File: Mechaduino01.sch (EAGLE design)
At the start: 68 parts, among them IC1 SAMD21G18A-AUT, IC2 AP2112K-3.3, Q1 2.5A/30V, Q2 NFET, Q3 BSS138, Q4 BSS138, SW1 SPST_TACT-KMR2, U3 74AHC1G125, Y1 32,768Khz

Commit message: Final
ordered
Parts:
- removed SW1: SPST_TACT-KMR2, adafruit:SPST_TACT-KMR2
- added SW2: (no value), MF_Switches:TACT_4.2MM
- C10, C18: device swift:CAP0402 -> rcl:C-USC0805
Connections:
- net GND: now also SW2.P$3, SW2.P$4; no longer SW1.P, SW1.P1
- net RESET: now also SW2.P$1, SW2.P$2; no longer SW1.S, SW1.S1
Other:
- moved on the sheet: C10, C18
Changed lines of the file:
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@@
 <part name="C4" library="swift" deviceset="CAP" device="0402" value="0.1uF"/>
 <part name="GND6" library="PowerTags" deviceset="GND" device=""/>
-<part name="SW1" library="adafruit" deviceset="SPST_TACT" device="-KMR2" value=""/>
 <part name="GND11" library="supply1" deviceset="GND" device=""/>
 <part name="D1" library="adafruit" deviceset="DIODE" device="SOD-523"/>
@@
 <part name="IC2" library="SparkFun-PowerIC" deviceset="AP2202-ADJ" device="" value="AP2112K-3.3"/>
 <part name="C9" library="swift" deviceset="CAP" device="0402" value="0.1uF"/>
-<part name="C10" library="swift" deviceset="CAP" device="0402" value="10.0uF"/>
+<part name="C10" library="rcl" deviceset="C-US" device="C0805" value="10.0uF"/>
 <part name="GND5" library="supply1" deviceset="GND" device=""/>
 <part name="GND7" library="supply1" deviceset="GND" device=""/>
@@
 <part name="R21" library="adafruit" deviceset="R-US_" device="R0402-VISHAY" value="10K"/>
 <part name="C6" library="swift" deviceset="CAP" device="0402" value="0.01uF"/>
-<part name="C18" library="swift" deviceset="CAP" device="0402" value="10.0uF"/>
+<part name="C18" library="rcl" deviceset="C-US" device="C0805" value="10.0uF"/>
 <part name="C19" library="swift" deviceset="CAP" device="0402" value="0.1uF"/>
 <part name="GND2" library="supply1" deviceset="GND" device=""/>
@@
 <part name="V+" library="MF_Connectors" deviceset="HEADER_01X03" device="_PTH_2.54MM"/>
 <part name="U$5" library="stepper_servo_prototype_1" deviceset="MECHADUINO_LOGO" device=""/>
+<part name="SW2" library="MF_Switches" deviceset="TACT" device="_4.2MM"/>
 </parts>
 <sheets>
@@
 </instance>
 <instance part="GND6" gate="1" x="22.86" y="215.9"/>
-<instance part="SW1" gate="G$1" x="337.82" y="215.9"/>
 <instance part="GND11" gate="1" x="337.82" y="205.74"/>
 <instance part="D1" gate="G$1" x="342.9" y="241.3" rot="R90"/>
@@
 <instance part="V+" gate="G$1" x="414.02" y="68.58" rot="MR0"/>
 <instance part="U$5" gate="G$1" x="259.08" y="7.62"/>
+<instance part="SW2" gate="G$1" x="342.9" y="218.44"/>
 </instances>
 <busses>
@@
 </segment>
 <segment>
-<pinref part="SW1" gate="G$1" pin="P"/>
-<pinref part="SW1" gate="G$1" pin="P1"/>
-<wire x1="337.82" y1="210.82" x2="340.36" y2="210.82" width="0.1524" layer="91"/>
 <wire x1="337.82" y1="210.82" x2="337.82" y2="208.28" width="0.1524" layer="91"/>
+<pinref part="GND11" gate="1" pin="GND"/>
+<pinref part="SW2" gate="G$1" pin="P$3"/>
+<pinref part="SW2" gate="G$1" pin="P$4"/>
+<wire x1="337.82" y1="210.82" x2="337.82" y2="215.9" width="0.1524" layer="91"/>
+<wire x1="337.82" y1="215.9" x2="347.98" y2="215.9" width="0.1524" layer="91"/>
 <junction x="337.82" y="210.82"/>
-<pinref part="GND11" gate="1" pin="GND"/>
+<junction x="337.82" y="215.9"/>
 </segment>
 <segment>
@@
 <pinref part="C10" gate="G$1" pin="2"/>
 <pinref part="GND5" gate="1" pin="GND"/>
-<wire x1="193.04" y1="45.72" x2="193.04" y2="48.26" width="0.1524" layer="91"/>
 </segment>
 <segment>
@@
 <pinref part="C18" gate="G$1" pin="2"/>
 <pinref part="GND2" gate="1" pin="GND"/>
-<wire x1="142.24" y1="48.26" x2="142.24" y2="45.72" width="0.1524" layer="91"/>
 </segment>
 <segment>
@@
 <junction x="337.82" y="233.68"/>
 <pinref part="R1" gate="G$1" pin="1"/>
-<pinref part="SW1" gate="G$1" pin="S1"/>
-<pinref part="SW1" gate="G$1" pin="S"/>
-<wire x1="340.36" y1="220.98" x2="337.82" y2="220.98" width="0.1524" layer="91"/>
-<wire x1="337.82" y1="220.98" x2="337.82" y2="226.06" width="0.1524" layer="91"/>
-<junction x="337.82" y="220.98"/>
 <junction x="337.82" y="226.06"/>
+<wire x1="337.82" y1="223.52" x2="337.82" y2="226.06" width="0.1524" layer="91"/>
 <wire x1="337.82" y1="233.68" x2="342.9" y2="233.68" width="0.1524" layer="91"/>
 <pinref part="D1" gate="G$1" pin="A"/>
 <wire x1="342.9" y1="233.68" x2="342.9" y2="238.76" width="0.1524" layer="91"/>
 <wire x1="337.82" y1="226.06" x2="325.12" y2="226.06" width="0.1524" layer="91"/>
+<pinref part="SW2" gate="G$1" pin="P$1"/>
+<pinref part="SW2" gate="G$1" pin="P$2"/>
+<wire x1="337.82" y1="223.52" x2="337.82" y2="220.98" width="0.1524" layer="91"/>
+<wire x1="337.82" y1="220.98" x2="347.98" y2="220.98" width="0.1524" layer="91"/>
+<junction x="337.82" y="223.52"/>
+<junction x="337.82" y="220.98"/>
 </segment>
 <segment>
@@
 <pinref part="C10" gate="G$1" pin="1"/>
 <pinref part="IC2" gate="G$1" pin="OUT"/>
-<wire x1="185.42" y1="55.88" x2="193.04" y2="55.88" width="0.1524" layer="91"/>
+<wire x1="185.42" y1="55.88" x2="193.04" y2="53.34" width="0.1524" layer="91"/>
 <pinref part="SUPPLY2" gate="G$1" pin="3.3V"/>
-<wire x1="193.04" y1="55.88" x2="203.2" y2="55.88" width="0.1524" layer="91"/>
+<wire x1="193.04" y1="53.34" x2="203.2" y2="55.88" width="0.1524" layer="91"/>
 <wire x1="203.2" y1="55.88" x2="213.36" y2="55.88" width="0.1524" layer="91"/>
 <wire x1="213.36" y1="55.88" x2="213.36" y2="60.96" width="0.1524" layer="91"/>
-<junction x="193.04" y="55.88"/>
+<junction x="193.04" y="53.34"/>
 <pinref part="C19" gate="G$1" pin="1"/>
 <junction x="203.2" y="55.88"/>
@@
 <pinref part="IC2" gate="G$1" pin="EN"/>
 <wire x1="165.1" y1="45.72" x2="167.64" y2="45.72" width="0.1524" layer="91"/>
-<wire x1="134.62" y1="55.88" x2="142.24" y2="55.88" width="0.1524" layer="91"/>
+<wire x1="134.62" y1="55.88" x2="142.24" y2="53.34" width="0.1524" layer="91"/>
 <pinref part="C18" gate="G$1" pin="1"/>
-<wire x1="142.24" y1="55.88" x2="149.86" y2="55.88" width="0.1524" layer="91"/>
-<junction x="142.24" y="55.88"/>
-</segment>
-<segment>
+<wire x1="142.24" y1="53.34" x2="149.86" y2="55.88" width="0.1524" layer="91"/>
+<junction x="142.24" y="53.34"/>
+</segment>
+<segment>

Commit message: updated readme
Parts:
- R12, R13: value .25 Ohm -> .15 Ohm
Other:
- moved on the sheet: C10, C18
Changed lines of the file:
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@@
 <part name="GND19" library="supply1" deviceset="GND" device=""/>
 <part name="U$1" library="avagopack" deviceset="AVAGO_DRIVER" device=""/>
-<part name="R12" library="adafruit" deviceset="R-US_" device="R1206" value=".25 Ohm"/>
-<part name="R13" library="adafruit" deviceset="R-US_" device="R1206" value=".25 Ohm"/>
+<part name="R12" library="adafruit" deviceset="R-US_" device="R1206" value=".15 Ohm"/>
+<part name="R13" library="adafruit" deviceset="R-US_" device="R1206" value=".15 Ohm"/>
 <part name="C12" library="SparkFun-Capacitors" deviceset="CAP_POL" device="D" value="100uF"/>
 <part name="C13" library="swift" deviceset="CAP" device="0603" value="1.0uF"/>
@@
 <instance part="IC2" gate="G$1" x="177.8" y="50.8"/>
 <instance part="C9" gate="G$1" x="149.86" y="50.8"/>
-<instance part="C10" gate="G$1" x="193.04" y="50.8"/>
+<instance part="C10" gate="G$1" x="193.04" y="53.34"/>
 <instance part="GND5" gate="1" x="193.04" y="43.18" smashed="yes">
 <attribute name="VALUE" x="190.5" y="40.64" size="1.778" layer="96"/>
@@
 <instance part="R21" gate="G$1" x="330.2" y="185.42" rot="R90"/>
 <instance part="C6" gate="G$1" x="144.78" y="109.22"/>
-<instance part="C18" gate="G$1" x="142.24" y="50.8"/>
+<instance part="C18" gate="G$1" x="142.24" y="53.34"/>
 <instance part="C19" gate="G$1" x="203.2" y="50.8"/>
 <instance part="GND2" gate="1" x="142.24" y="43.18" smashed="yes">
@@
 <pinref part="C10" gate="G$1" pin="2"/>
 <pinref part="GND5" gate="1" pin="GND"/>
+<wire x1="193.04" y1="48.26" x2="193.04" y2="45.72" width="0.1524" layer="91"/>
 </segment>
 <segment>
@@
 <pinref part="C18" gate="G$1" pin="2"/>
 <pinref part="GND2" gate="1" pin="GND"/>
+<wire x1="142.24" y1="48.26" x2="142.24" y2="45.72" width="0.1524" layer="91"/>
 </segment>
 <segment>
@@
 <pinref part="C10" gate="G$1" pin="1"/>
 <pinref part="IC2" gate="G$1" pin="OUT"/>
-<wire x1="185.42" y1="55.88" x2="193.04" y2="53.34" width="0.1524" layer="91"/>
+<wire x1="185.42" y1="55.88" x2="193.04" y2="55.88" width="0.1524" layer="91"/>
 <pinref part="SUPPLY2" gate="G$1" pin="3.3V"/>
-<wire x1="193.04" y1="53.34" x2="203.2" y2="55.88" width="0.1524" layer="91"/>
+<wire x1="193.04" y1="55.88" x2="203.2" y2="55.88" width="0.1524" layer="91"/>
 <wire x1="203.2" y1="55.88" x2="213.36" y2="55.88" width="0.1524" layer="91"/>
 <wire x1="213.36" y1="55.88" x2="213.36" y2="60.96" width="0.1524" layer="91"/>
-<junction x="193.04" y="53.34"/>
+<junction x="193.04" y="55.88"/>
 <pinref part="C19" gate="G$1" pin="1"/>
 <junction x="203.2" y="55.88"/>
@@
 <pinref part="IC2" gate="G$1" pin="EN"/>
 <wire x1="165.1" y1="45.72" x2="167.64" y2="45.72" width="0.1524" layer="91"/>
-<wire x1="134.62" y1="55.88" x2="142.24" y2="53.34" width="0.1524" layer="91"/>
+<wire x1="134.62" y1="55.88" x2="142.24" y2="55.88" width="0.1524" layer="91"/>
 <pinref part="C18" gate="G$1" pin="1"/>
-<wire x1="142.24" y1="53.34" x2="149.86" y2="55.88" width="0.1524" layer="91"/>
-<junction x="142.24" y="53.34"/>
-</segment>
-<segment>
+<wire x1="142.24" y1="55.88" x2="149.86" y2="55.88" width="0.1524" layer="91"/>
+<junction x="142.24" y="55.88"/>
+</segment>
+<segment>

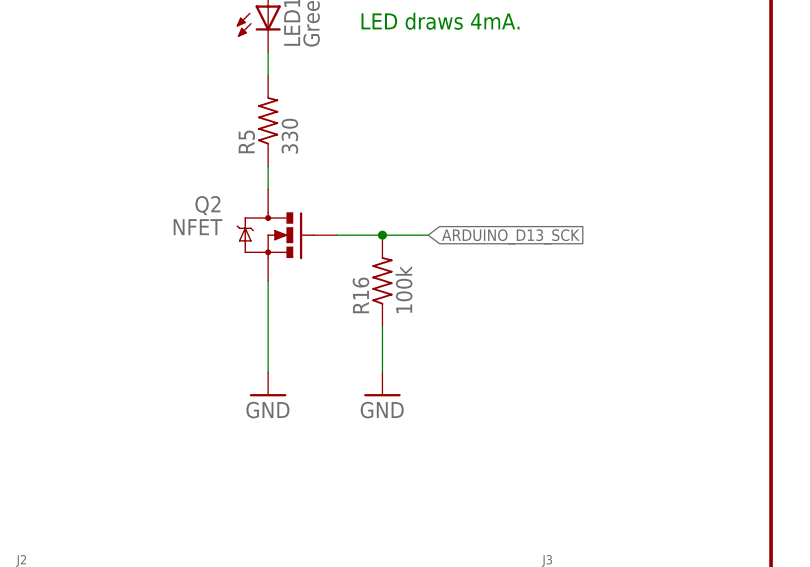
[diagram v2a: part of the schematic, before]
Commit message: Fix case sensitivity on 100k res
Case sensitivity in BOM export causes 2 seperate entries in the BOM
under the 100k resistors.  Ks are mostly capitalized throughout the
schematic, so corrected this one.
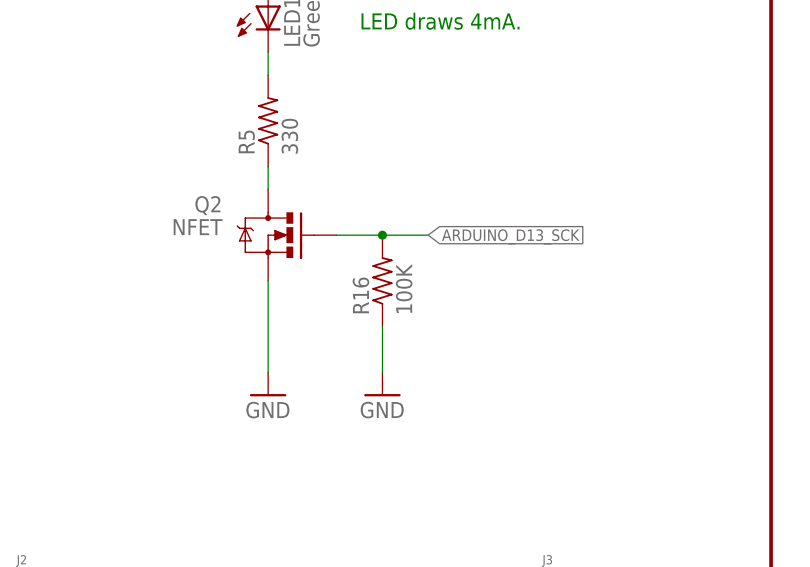
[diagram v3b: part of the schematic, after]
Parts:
- R16: value 100k -> 100K
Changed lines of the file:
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@@
 <part name="J1" library="MF_Connectors" deviceset="USB" device="_MICRO_RIGHT"/>
 <part name="FRAME1" library="SparkFun-Aesthetics" deviceset="FRAME-LEDGER" device=""/>
-<part name="R16" library="adafruit" deviceset="R-US_" device="R0402-VISHAY" value="100k"/>
+<part name="R16" library="adafruit" deviceset="R-US_" device="R0402-VISHAY" value="100K"/>
 <part name="GND20" library="supply1" deviceset="GND" device=""/>
 <part name="F1" library="SparkFun-PowerIC" deviceset="PTC" device="SMD" value="500mA"/>

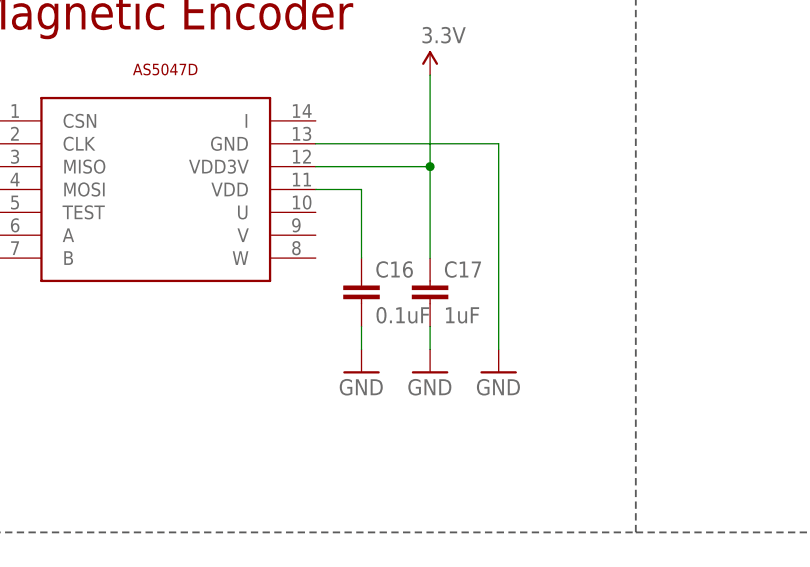
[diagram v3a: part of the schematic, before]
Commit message: minor change to as5047 power circuit
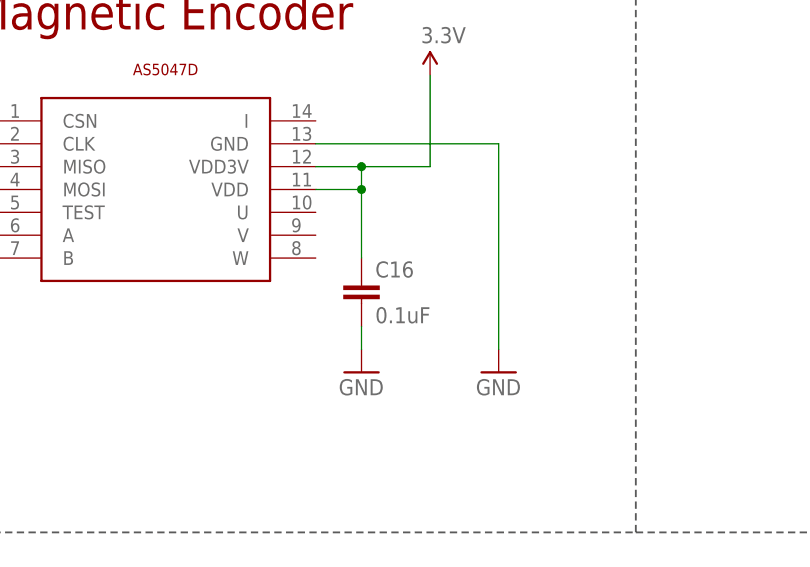
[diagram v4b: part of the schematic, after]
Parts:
- removed C17: 1uF, swift:CAP0402
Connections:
- removed net N$27: C16.1, U$4.VDD
- net 3.3V: now also C16.1, U$4.VDD; no longer C17.1
- net GND: no longer C17.2
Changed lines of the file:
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@@
 <?xml version="1.0" encoding="utf-8"?>
 <!DOCTYPE eagle SYSTEM "eagle.dtd">
-<eagle version="7.3.0">
+<eagle version="7.7.0">
 <drawing>
 <settings>
@@
 <part name="GND22" library="supply1" deviceset="GND" device=""/>
 <part name="C16" library="swift" deviceset="CAP" device="0402" value="0.1uF"/>
-<part name="C17" library="swift" deviceset="CAP" device="0402" value="1uF"/>
 <part name="GND23" library="supply1" deviceset="GND" device=""/>
-<part name="GND24" library="supply1" deviceset="GND" device=""/>
 <part name="SUPPLY16" library="supply2" deviceset="GND2" device=""/>
 <part name="SUPPLY17" library="supply2" deviceset="GND2" device=""/>
@@
 <instance part="GND22" gate="1" x="218.44" y="104.14"/>
 <instance part="C16" gate="G$1" x="264.16" y="111.76"/>
-<instance part="C17" gate="G$1" x="271.78" y="111.76"/>
 <instance part="GND23" gate="1" x="264.16" y="104.14"/>
-<instance part="GND24" gate="1" x="271.78" y="104.14"/>
 <instance part="SUPPLY16" gate="G$1" x="48.26" y="96.52"/>
 <instance part="SUPPLY17" gate="G$1" x="55.88" y="96.52"/>
@@
 <pinref part="GND23" gate="1" pin="GND"/>
 <wire x1="264.16" y1="106.68" x2="264.16" y2="109.22" width="0.1524" layer="91"/>
-</segment>
-<segment>
-<pinref part="C17" gate="G$1" pin="2"/>
-<pinref part="GND24" gate="1" pin="GND"/>
-<wire x1="271.78" y1="106.68" x2="271.78" y2="109.22" width="0.1524" layer="91"/>
 </segment>
 <segment>
@@
 <segment>
 <pinref part="U$4" gate="G$1" pin="VDD3V"/>
-<wire x1="259.08" y1="127" x2="271.78" y2="127" width="0.1524" layer="91"/>
-<pinref part="C17" gate="G$1" pin="1"/>
-<wire x1="271.78" y1="116.84" x2="271.78" y2="127" width="0.1524" layer="91"/>
-<junction x="271.78" y="127"/>
+<wire x1="259.08" y1="127" x2="264.16" y2="127" width="0.1524" layer="91"/>
 <pinref part="SUPPLY21" gate="G$1" pin="3.3V"/>
+<wire x1="264.16" y1="127" x2="271.78" y2="127" width="0.1524" layer="91"/>
 <wire x1="271.78" y1="127" x2="271.78" y2="137.16" width="0.1524" layer="91"/>
+<pinref part="U$4" gate="G$1" pin="VDD"/>
+<wire x1="259.08" y1="124.46" x2="264.16" y2="124.46" width="0.1524" layer="91"/>
+<pinref part="C16" gate="G$1" pin="1"/>
+<wire x1="264.16" y1="116.84" x2="264.16" y2="124.46" width="0.1524" layer="91"/>
+<wire x1="264.16" y1="124.46" x2="264.16" y2="127" width="0.1524" layer="91"/>
+<junction x="264.16" y="124.46"/>
+<junction x="264.16" y="127"/>
 </segment>
 <segment>
@@
 </segment>
 </net>
-<net name="N$27" class="0">
-<segment>
-<pinref part="U$4" gate="G$1" pin="VDD"/>
-<wire x1="259.08" y1="124.46" x2="264.16" y2="124.46" width="0.1524" layer="91"/>
-<pinref part="C16" gate="G$1" pin="1"/>
-<wire x1="264.16" y1="116.84" x2="264.16" y2="124.46" width="0.1524" layer="91"/>
-</segment>
-</net>

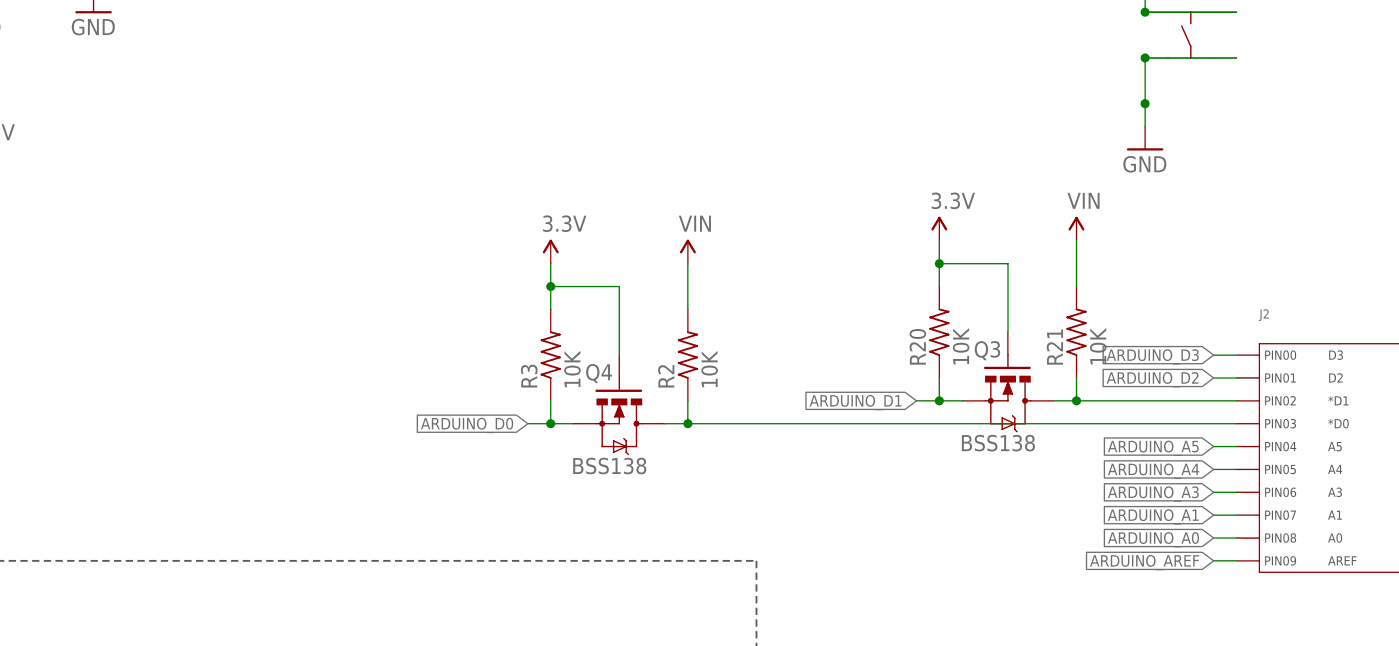
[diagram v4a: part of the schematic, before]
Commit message: added third level shifter (same as others)
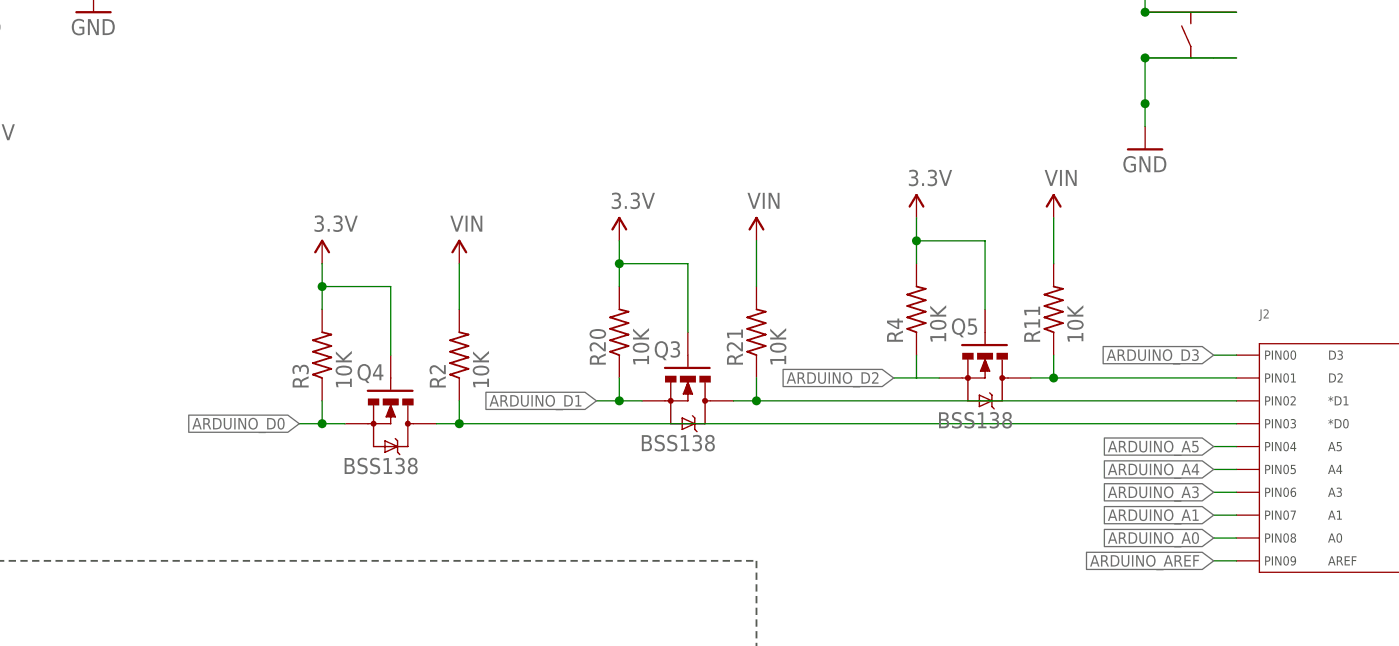
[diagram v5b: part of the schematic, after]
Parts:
- added Q5: BSS138, SparkFun:MOSFET-NCHANNELSMD
- added R11, R4: 10K, adafruit:R-US_R0402-VISHAY
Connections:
- new net HV3: J2.PIN1, Q5.D, R11.1
- net 3.3V: now also Q5.G, R4.2
- net ARDUINO_D2: now also Q5.S, R4.1; no longer J2.PIN1
- net VIN: now also R11.2
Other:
- moved on the sheet: Q3, Q4, R2, R20, R21, R3
